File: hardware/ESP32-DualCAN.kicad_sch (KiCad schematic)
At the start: 31 parts, among them J1 Molex 70553 6p, J2 Conn_01x10_Socket, J3 Conn_01x10_Socket, J4 holes, J5 pads, J6 holes, J7 pads, U1 LV2862Y, U2 ESP32-C6-SuperMini, U3 TCAN1044AV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

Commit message: kicad 10
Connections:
- net CAN0_H: now also J1.6 (Pin_6), J4.6 (Pin_6), J5.6 (Pin_6), J6.6 (Pin_6), J7.6 (Pin_6); no longer J1.5 (Pin_5), J4.5 (Pin_5), J5.5 (Pin_5), J6.5 (Pin_5), J7.5 (Pin_5)
- net CAN0_L: now also J1.5 (Pin_5), J4.5 (Pin_5), J5.5 (Pin_5), J6.5 (Pin_5), J7.5 (Pin_5); no longer J1.6 (Pin_6), J4.6 (Pin_6), J5.6 (Pin_6), J6.6 (Pin_6), J7.6 (Pin_6)
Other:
- note added: "Vbat Gnd ChassisCAN L ChassisCAN H VehicleCAN L VehicleCAN H"
- note removed: "Vbat Gnd ChassisCAN L ChassisCAN H VehicleCAN H VehicleCAN L"

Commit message: update pcb
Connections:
- net CAN0_H: now also J1.5 (Pin_5), J4.5 (Pin_5), J5.5 (Pin_5), J6.5 (Pin_5), J7.5 (Pin_5); no longer J1.6 (Pin_6), J4.6 (Pin_6), J5.6 (Pin_6), J6.6 (Pin_6), J7.6 (Pin_6)
- net CAN0_L: now also J1.6 (Pin_6), J4.6 (Pin_6), J5.6 (Pin_6), J6.6 (Pin_6), J7.6 (Pin_6); no longer J1.5 (Pin_5), J4.5 (Pin_5), J5.5 (Pin_5), J6.5 (Pin_5), J7.5 (Pin_5)
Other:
- note added: "Vbat Gnd ChassisCAN L ChassisCAN H VehicleCAN H VehicleCAN L"
- note removed: "Vbat Gnd ChassisCAN L ChassisCAN H VehicleCAN L VehicleCAN H"
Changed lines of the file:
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@@
 		)
 	)
-	(text "Vbat\nGnd\nChassisCAN L\nChassisCAN H\nVehicleCAN L\nVehicleCAN H"
+	(text "Vbat\nGnd\nChassisCAN L\nChassisCAN H\nVehicleCAN H\nVehicleCAN L"
 		(exclude_from_sim no)
 		(at 92.964 185.674 0)
@@
 		)
 	)
-	(global_label "CAN0_L"
+	(global_label "CAN0_H"
 		(shape bidirectional)
 		(at 49.53 189.23 180)
@@
 		)
 		(property "Intersheetrefs" "${INTERSHEET_REFS}"
-			(at 38.5392 189.23 0)
+			(at 38.2368 189.23 0)
 			(hide yes)
 			(show_name no)
@@
 		)
 	)
-	(global_label "CAN0_H"
+	(global_label "CAN0_L"
 		(shape bidirectional)
 		(at 49.53 191.77 180)
@@
 		)
 		(property "Intersheetrefs" "${INTERSHEET_REFS}"
-			(at 38.2368 191.77 0)
+			(at 38.5392 191.77 0)
 			(hide yes)
 			(show_name no)
@@
 		(in_bom no)
 		(on_board yes)
-		(in_pos_files yes)
+		(in_pos_files no)
 		(dnp no)
 		(property "Reference" "J5"
@@
 		(in_bom no)
 		(on_board yes)
-		(in_pos_files yes)
+		(in_pos_files no)
 		(dnp no)
 		(property "Reference" "J6"
@@
 		(in_bom no)
 		(on_board yes)
-		(in_pos_files yes)
+		(in_pos_files no)
 		(dnp no)
 		(property "Reference" "J7"
@@
 		(in_bom no)
 		(on_board yes)
-		(in_pos_files yes)
+		(in_pos_files no)
 		(dnp no)
 		(property "Reference" "J4"

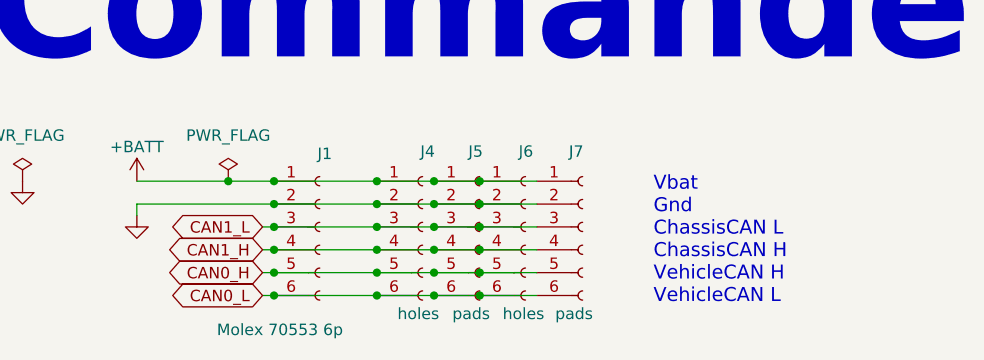
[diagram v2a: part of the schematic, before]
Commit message: fix: flipped VehicleCAN pins
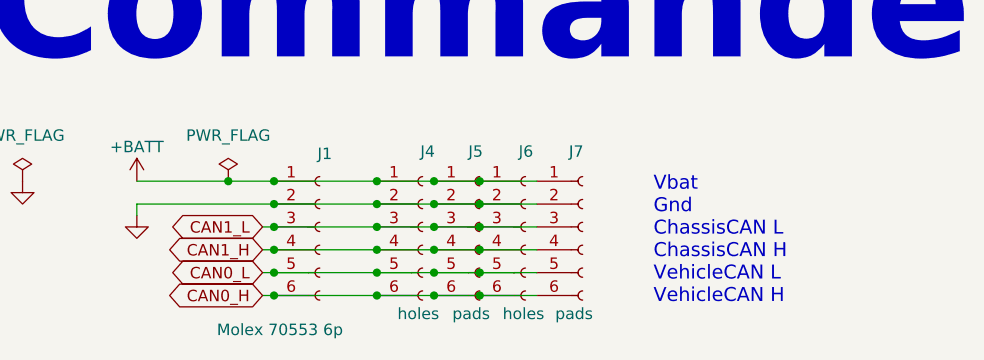
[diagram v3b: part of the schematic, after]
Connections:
- net CAN0_H: now also J1.6 (Pin_6), J4.6 (Pin_6), J5.6 (Pin_6), J6.6 (Pin_6), J7.6 (Pin_6); no longer J1.5 (Pin_5), J4.5 (Pin_5), J5.5 (Pin_5), J6.5 (Pin_5), J7.5 (Pin_5)
- net CAN0_L: now also J1.5 (Pin_5), J4.5 (Pin_5), J5.5 (Pin_5), J6.5 (Pin_5), J7.5 (Pin_5); no longer J1.6 (Pin_6), J4.6 (Pin_6), J5.6 (Pin_6), J6.6 (Pin_6), J7.6 (Pin_6)
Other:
- note added: "Vbat Gnd ChassisCAN L ChassisCAN H VehicleCAN L VehicleCAN H"
- note removed: "Vbat Gnd ChassisCAN L ChassisCAN H VehicleCAN H VehicleCAN L"
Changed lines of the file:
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@@
 		)
 	)
-	(text "Vbat\nGnd\nChassisCAN L\nChassisCAN H\nVehicleCAN H\nVehicleCAN L"
+	(text "Vbat\nGnd\nChassisCAN L\nChassisCAN H\nVehicleCAN L\nVehicleCAN H"
 		(exclude_from_sim no)
 		(at 92.964 185.674 0)
@@
 		)
 	)
-	(global_label "CAN0_H"
+	(global_label "CAN0_L"
 		(shape bidirectional)
 		(at 49.53 189.23 180)
@@
 		)
 		(property "Intersheetrefs" "${INTERSHEET_REFS}"
-			(at 38.2368 189.23 0)
+			(at 38.5392 189.23 0)
 			(hide yes)
 			(show_name no)
@@
 		)
 	)
-	(global_label "CAN0_L"
+	(global_label "CAN0_H"
 		(shape bidirectional)
 		(at 49.53 191.77 180)
@@
 		)
 		(property "Intersheetrefs" "${INTERSHEET_REFS}"
-			(at 38.5392 191.77 0)
+			(at 38.2368 191.77 0)
 			(hide yes)
 			(show_name no)
